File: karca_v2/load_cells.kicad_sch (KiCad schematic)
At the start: 4 parts, among them J3 Screw_Terminal_01x08, J4 Screw_Terminal_01x08, U3 MCP3208

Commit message: updated
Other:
- moved on the sheet: C6, J3, J4, U3

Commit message: Version alpha
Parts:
- added C66, C67, C68, C69: 0.1u, Capacitor_SMD:C_1206_3216Metric, symbol Device:C
- added RV1: 30k, Potentiometer_THT:Potentiometer_Bourns_3296W_Vertical, symbol Device:R_Potentiometer
- added TP6, TP7, TP8, TP9: TestPoint, TestPoint:TestPoint_Pad_D2.0mm, symbol Connector:TestPoint
- added U3: NUP4202, Package_SO:TSOP-6_1.65x3.05mm_P0.95mm, symbol Power_Protection:NUP4202
- added U4, U5: TLV9304xD, Package_SO:SO-14_3.9x8.65mm_P1.27mm, symbol Amplifier_Operational:TLV9304xD
- J4: renamed from J3; value Screw_Terminal_01x08 -> LoadCell_1_2; footprint (none) -> terminal blocks:P-2604-1108
- J5: renamed from J4; value Screw_Terminal_01x08 -> LoadCell_3_4; footprint (none) -> terminal blocks:P-2604-1108
- U2: renamed from U3; footprint (none) -> Package_SO:SOIC-16_3.9x9.9mm_P1.27mm
- renumbered C6 to C2
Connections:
- net +5V: now also C66.2, C68.2, RV1.3, U3.5, U4.4 (V+), U5.4 (V+)
- net GND: now also C66.1, C67.1, C67.2, C68.1, C69.1, C69.2, RV1.1, U3.2, U4.11 (V-), U5.11 (V-)
- net LC_Amplification/OUT: now also TP6.1, U3.6
- net LC_Amplification1/OUT: now also TP7.1, U3.4
- net LC_Amplification2/OUT: now also TP8.1, U3.1
- net LC_Amplification3/OUT: now also TP9.1, U3.3
- net DRV1_ADC: now reaches U2.5 (CH4)
- net DRV2_ADC: now reaches U2.6 (CH5)
- net DRV3_ADC: now reaches U2.7 (CH6)
- net DRV4_ADC: now reaches U2.8 (CH7)
- new net IN_AMP_VREF: RV1.2
- no-connect marks 4 -> 0
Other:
- sheet LC_Amplification ports: added INAMP_VREF; removed none
- sheet LC_Amplification1 ports: added INAMP_VREF; removed none
- sheet LC_Amplification2 ports: added INAMP_VREF; removed none
- sheet LC_Amplification3 ports: added INAMP_VREF; removed none
- moved on the sheet: C2, J4, J5, U2

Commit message: fkkkkkkkkkk
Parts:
- U3: footprint Package_SO:TSOP-6_1.65x3.05mm_P0.95mm -> Package_TO_SOT_SMD:SOT-363_SC-70-6
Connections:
- net DRV1_ADC is gone; now on net LC_Amplification/OUT: U2.5 (CH4)
- net DRV2_ADC is gone; now on net LC_Amplification1/OUT: U2.6 (CH5)
- net DRV3_ADC is gone; now on net LC_Amplification2/OUT: U2.7 (CH6)
- net DRV4_ADC is gone; now on net LC_Amplification3/OUT: U2.8 (CH7)
- net LC_Amplification/OUT: now also U3.4; no longer U2.1 (CH0), U3.6
- net LC_Amplification1/OUT: now also U3.6; no longer U2.2 (CH1), U3.4
- net LC_Amplification2/OUT: no longer U2.3 (CH2)
- net LC_Amplification3/OUT: no longer U2.4 (CH3)
- new net TC_1_ADC: U2.3 (CH2)
- new net TC_2_ADC: U2.4 (CH3)
- new net TC_3_ADC: U2.1 (CH0)
- new net TC_4_ADC: U2.2 (CH1)

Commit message: discrete traces
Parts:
- renumbered C2 to C3, C66 to C4, C68 to C5, C67 to C6, C69 to C7
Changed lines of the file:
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@@
   (symbol (lib_id "power:GND") (at 80.645 170.18 0) (unit 1)
     (in_bom yes) (on_board yes) (dnp no) (fields_autoplaced)
-    (property "Reference" "#PWR0197" (at 80.645 176.53 0)
+    (property "Reference" "#PWR028" (at 80.645 176.53 0)
       (effects (font (size 1.27 1.27)) hide)
     )
@@
       (project "karca_v2"
         (path "/29cf4797-56f2-4f57-ae95-7df639362e3c/ddbef897-b93d-4056-8606-b8e89931524a"
-          (reference "#PWR0197") (unit 1)
+          (reference "#PWR028") (unit 1)
         )
       )
@@
   (symbol (lib_id "power:GND") (at 41.275 184.15 0) (unit 1)
     (in_bom yes) (on_board yes) (dnp no) (fields_autoplaced)
-    (property "Reference" "#PWR0195" (at 41.275 190.5 0)
+    (property "Reference" "#PWR030" (at 41.275 190.5 0)
       (effects (font (size 1.27 1.27)) hide)
     )
@@
       (project "karca_v2"
         (path "/29cf4797-56f2-4f57-ae95-7df639362e3c/ddbef897-b93d-4056-8606-b8e89931524a"
-          (reference "#PWR0195") (unit 1)
+          (reference "#PWR030") (unit 1)
         )
       )
@@
   (symbol (lib_id "power:GND") (at 83.82 68.58 0) (unit 1)
     (in_bom yes) (on_board yes) (dnp no) (fields_autoplaced)
-    (property "Reference" "#PWR016" (at 83.82 74.93 0)
+    (property "Reference" "#PWR017" (at 83.82 74.93 0)
       (effects (font (size 1.27 1.27)) hide)
     )
@@
       (project "karca_v2"
         (path "/29cf4797-56f2-4f57-ae95-7df639362e3c/ddbef897-b93d-4056-8606-b8e89931524a"
-          (reference "#PWR016") (unit 1)
+          (reference "#PWR017") (unit 1)
         )
       )
@@
   (symbol (lib_id "power:+5V") (at 87.63 35.306 0) (unit 1)
     (in_bom yes) (on_board yes) (dnp no) (fields_autoplaced)
-    (property "Reference" "#PWR014" (at 87.63 39.116 0)
+    (property "Reference" "#PWR015" (at 87.63 39.116 0)
       (effects (font (size 1.27 1.27)) hide)
     )
@@
       (project "karca_v2"
         (path "/29cf4797-56f2-4f57-ae95-7df639362e3c/ddbef897-b93d-4056-8606-b8e89931524a"
-          (reference "#PWR014") (unit 1)
+          (reference "#PWR015") (unit 1)
         )
       )
@@
   (symbol (lib_id "power:+5V") (at 46.355 158.75 0) (unit 1)
     (in_bom yes) (on_board yes) (dnp no) (fields_autoplaced)
-    (property "Reference" "#PWR020" (at 46.355 162.56 0)
+    (property "Reference" "#PWR026" (at 46.355 162.56 0)
       (effects (font (size 1.27 1.27)) hide)
     )
@@
       (project "karca_v2"
         (path "/29cf4797-56f2-4f57-ae95-7df639362e3c/ddbef897-b93d-4056-8606-b8e89931524a"
-          (reference "#PWR020") (unit 1)
+          (reference "#PWR026") (unit 1)
         )
       )
@@
   (symbol (lib_id "power:+5V") (at 74.93 85.09 0) (unit 1)
     (in_bom yes) (on_board yes) (dnp no) (fields_autoplaced)
-    (property "Reference" "#PWR018" (at 74.93 88.9 0)
+    (property "Reference" "#PWR019" (at 74.93 88.9 0)
       (effects (font (size 1.27 1.27)) hide)
     )
@@
       (project "karca_v2"
         (path "/29cf4797-56f2-4f57-ae95-7df639362e3c/ddbef897-b93d-4056-8606-b8e89931524a"
-          (reference "#PWR018") (unit 1)
+          (reference "#PWR019") (unit 1)
         )
       )
@@
   (symbol (lib_id "power:GND") (at 81.28 142.24 0) (unit 1)
     (in_bom yes) (on_board yes) (dnp no) (fields_autoplaced)
-    (property "Reference" "#PWR026" (at 81.28 148.59 0)
+    (property "Reference" "#PWR025" (at 81.28 148.59 0)
       (effects (font (size 1.27 1.27)) hide)
     )
@@
       (project "karca_v2"
         (path "/29cf4797-56f2-4f57-ae95-7df639362e3c/ddbef897-b93d-4056-8606-b8e89931524a"
-          (reference "#PWR026") (unit 1)
+          (reference "#PWR025") (unit 1)
         )
       )
@@
   (symbol (lib_id "Device:C") (at 38.735 162.56 180) (unit 1)
     (in_bom yes) (on_board yes) (dnp no)
-    (property "Reference" "C66" (at 32.385 161.29 0)
+    (property "Reference" "C4" (at 32.385 161.29 0)
       (effects (font (size 1.27 1.27)) (justify right))
     )
@@
       (project "karca_v2"
         (path "/29cf4797-56f2-4f57-ae95-7df639362e3c/ddbef897-b93d-4056-8606-b8e89931524a"
-          (reference "C66") (unit 1)
+          (reference "C4") (unit 1)
         )
       )
@@
   (symbol (lib_id "Device:C") (at 245.11 66.04 90) (unit 1)
     (in_bom yes) (on_board yes) (dnp no) (fields_autoplaced)
-    (property "Reference" "C2" (at 245.11 58.42 90)
+    (property "Reference" "C3" (at 245.11 58.42 90)
       (effects (font (size 1.27 1.27)))
     )
@@
       (project "karca_v2"
         (path "/29cf4797-56f2-4f57-ae95-7df639362e3c/ddbef897-b93d-4056-8606-b8e89931524a"
-          (reference "C2") (unit 1)
+          (reference "C3") (unit 1)
         )
       )
@@
   (symbol (lib_id "power:GND") (at 80.645 186.69 0) (unit 1)
     (in_bom yes) (on_board yes) (dnp no) (fields_autoplaced)
-    (property "Reference" "#PWR0196" (at 80.645 193.04 0)
+    (property "Reference" "#PWR031" (at 80.645 193.04 0)
       (effects (font (size 1.27 1.27)) hide)
     )
@@
       (project "karca_v2"
         (path "/29cf4797-56f2-4f57-ae95-7df639362e3c/ddbef897-b93d-4056-8606-b8e89931524a"
-          (reference "#PWR0196") (unit 1)
+          (reference "#PWR031") (unit 1)
         )
       )
@@
   (symbol (lib_id "Device:C") (at 41.275 180.34 180) (unit 1)
     (in_bom yes) (on_board yes) (dnp no)
-    (property "Reference" "C67" (at 34.29 179.07 0)
+    (property "Reference" "C6" (at 34.29 179.07 0)
       (effects (font (size 1.27 1.27)) (justify right))
     )
@@
       (project "karca_v2"
         (path "/29cf4797-56f2-4f57-ae95-7df639362e3c/ddbef897-b93d-4056-8606-b8e89931524a"
-          (reference "C67") (unit 1)
+          (reference "C6") (unit 1)
         )
       )
@@
   (symbol (lib_id "power:GND") (at 252.73 68.58 0) (unit 1)
     (in_bom yes) (on_board yes) (dnp no) (fields_autoplaced)
-    (property "Reference" "#PWR017" (at 252.73 74.93 0)
+    (property "Reference" "#PWR018" (at 252.73 74.93 0)
       (effects (font (size 1.27 1.27)) hide)
     )
@@
       (project "karca_v2"
         (path "/29cf4797-56f2-4f57-ae95-7df639362e3c/ddbef897-b93d-4056-8606-b8e89931524a"
-          (reference "#PWR017") (unit 1)
+          (reference "#PWR018") (unit 1)
         )
       )
@@
   (symbol (lib_id "power:GND") (at 46.355 178.308 0) (unit 1)
     (in_bom yes) (on_board yes) (dnp no) (fields_autoplaced)
-    (property "Reference" "#PWR025" (at 46.355 184.658 0)
+    (property "Reference" "#PWR029" (at 46.355 184.658 0)
       (effects (font (size 1.27 1.27)) hide)
     )
@@
       (project "karca_v2"
         (path "/29cf4797-56f2-4f57-ae95-7df639362e3c/ddbef897-b93d-4056-8606-b8e89931524a"
-          (reference "#PWR025") (unit 1)
+          (reference "#PWR029") (unit 1)
         )
       )
@@
   (symbol (lib_id "Device:C") (at 80.645 182.88 180) (unit 1)
     (in_bom yes) (on_board yes) (dnp no)
-    (property "Reference" "C69" (at 74.295 181.61 0)
+    (property "Reference" "C7" (at 74.295 181.61 0)
       (effects (font (size 1.27 1.27)) (justify right))
     )
@@
       (project "karca_v2"
         (path "/29cf4797-56f2-4f57-ae95-7df639362e3c/ddbef897-b93d-4056-8606-b8e89931524a"
-          (reference "C69") (unit 1)
+          (reference "C7") (unit 1)
         )
       )
@@
   (symbol (lib_id "power:+5V") (at 229.87 64.77 0) (unit 1)
     (in_bom yes) (on_board yes) (dnp no) (fields_autoplaced)
-    (property "Reference" "#PWR015" (at 229.87 68.58 0)
+    (property "Reference" "#PWR016" (at 229.87 68.58 0)
       (effects (font (size 1.27 1.27)) hide)
     )
@@
       (project "karca_v2"
         (path "/29cf4797-56f2-4f57-ae95-7df639362e3c/ddbef897-b93d-4056-8606-b8e89931524a"
-          (reference "#PWR015") (unit 1)
+          (reference "#PWR016") (unit 1)
         )
       )
@@
   (symbol (lib_id "power:+5V") (at 186.69 88.9 0) (unit 1)
     (in_bom yes) (on_board yes) (dnp no) (fields_autoplaced)
-    (property "Reference" "#PWR019" (at 186.69 92.71 0)
+    (property "Reference" "#PWR020" (at 186.69 92.71 0)
       (effects (font (size 1.27 1.27)) hide)
     )
@@
       (project "karca_v2"
         (path "/29cf4797-56f2-4f57-ae95-7df639362e3c/ddbef897-b93d-4056-8606-b8e89931524a"
-          (reference "#PWR019") (unit 1)
+          (reference "#PWR020") (unit 1)
         )
       )
@@
   (symbol (lib_id "power:GND") (at 38.735 166.37 0) (unit 1)
     (in_bom yes) (on_board yes) (dnp no) (fields_autoplaced)
-    (property "Reference" "#PWR0194" (at 38.735 172.72 0)
+    (property "Reference" "#PWR027" (at 38.735 172.72 0)
       (effects (font (size 1.27 1.27)) hide)
     )
@@
       (project "karca_v2"
         (path "/29cf4797-56f2-4f57-ae95-7df639362e3c/ddbef897-b93d-4056-8606-b8e89931524a"
-          (reference "#PWR0194") (unit 1)
+          (reference "#PWR027") (unit 1)
         )
       )
@@
   (symbol (lib_id "Device:C") (at 80.645 166.37 180) (unit 1)
     (in_bom yes) (on_board yes) (dnp no)
-    (property "Reference" "C68" (at 74.295 165.1 0)
+    (property "Reference" "C5" (at 74.295 165.1 0)
       (effects (font (size 1.27 1.27)) (justify right))
     )
@@
       (project "karca_v2"
         (path "/29cf4797-56f2-4f57-ae95-7df639362e3c/ddbef897-b93d-4056-8606-b8e89931524a"
-          (reference "C68") (unit 1)
-        )
-      )
+          (reference "C5") (unit 1)
+        )
+      )

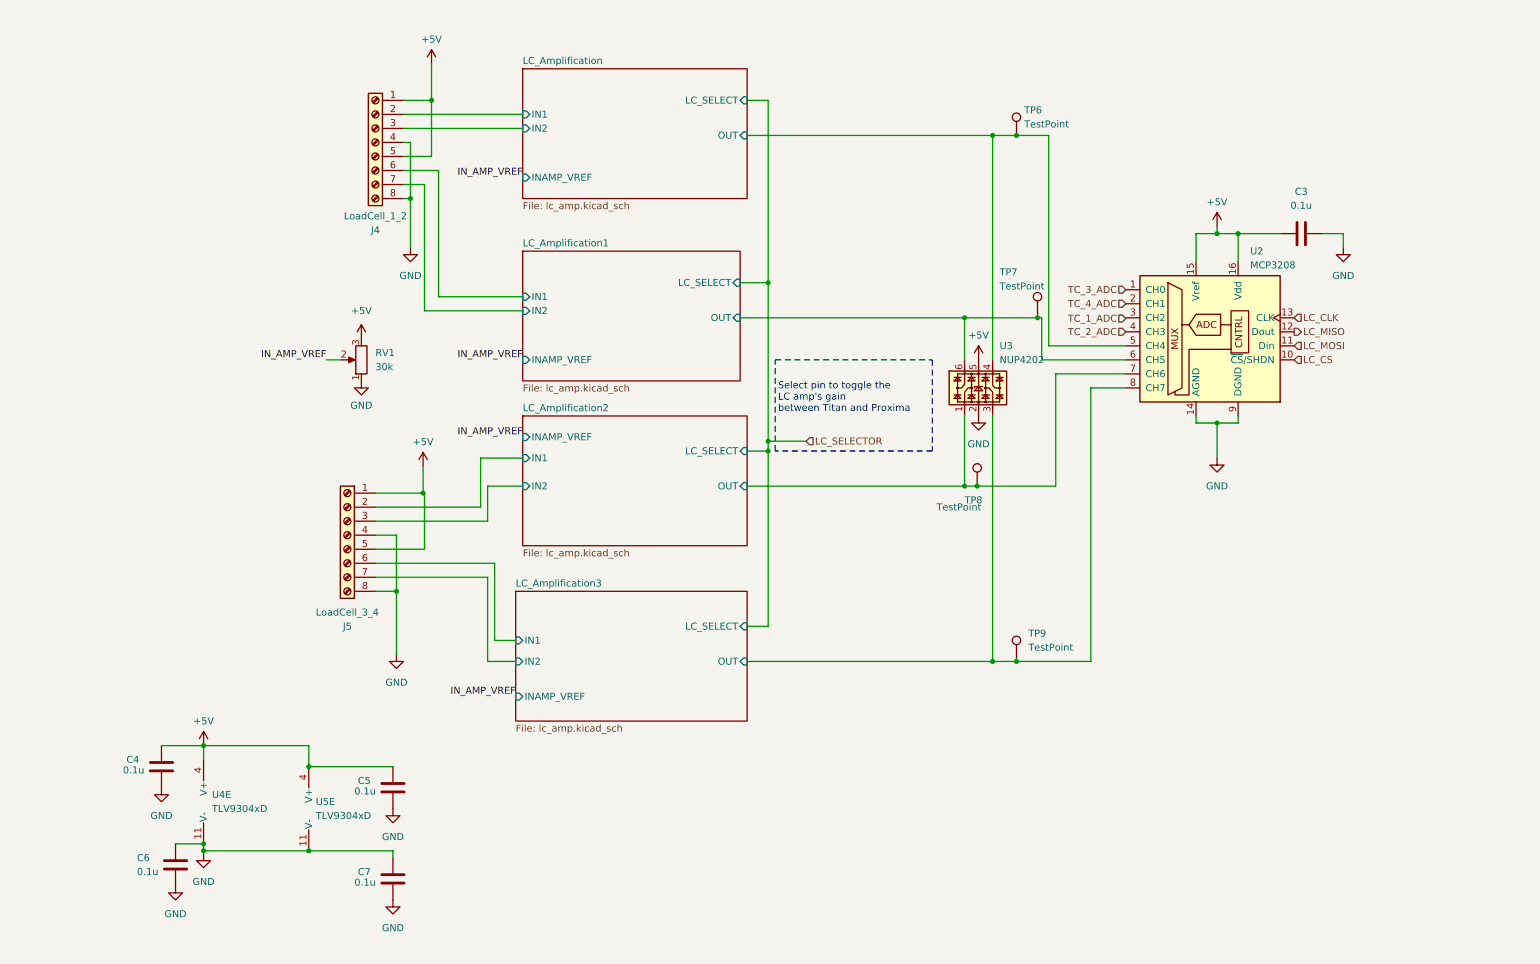
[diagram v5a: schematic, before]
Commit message: fixed TVS Diodes
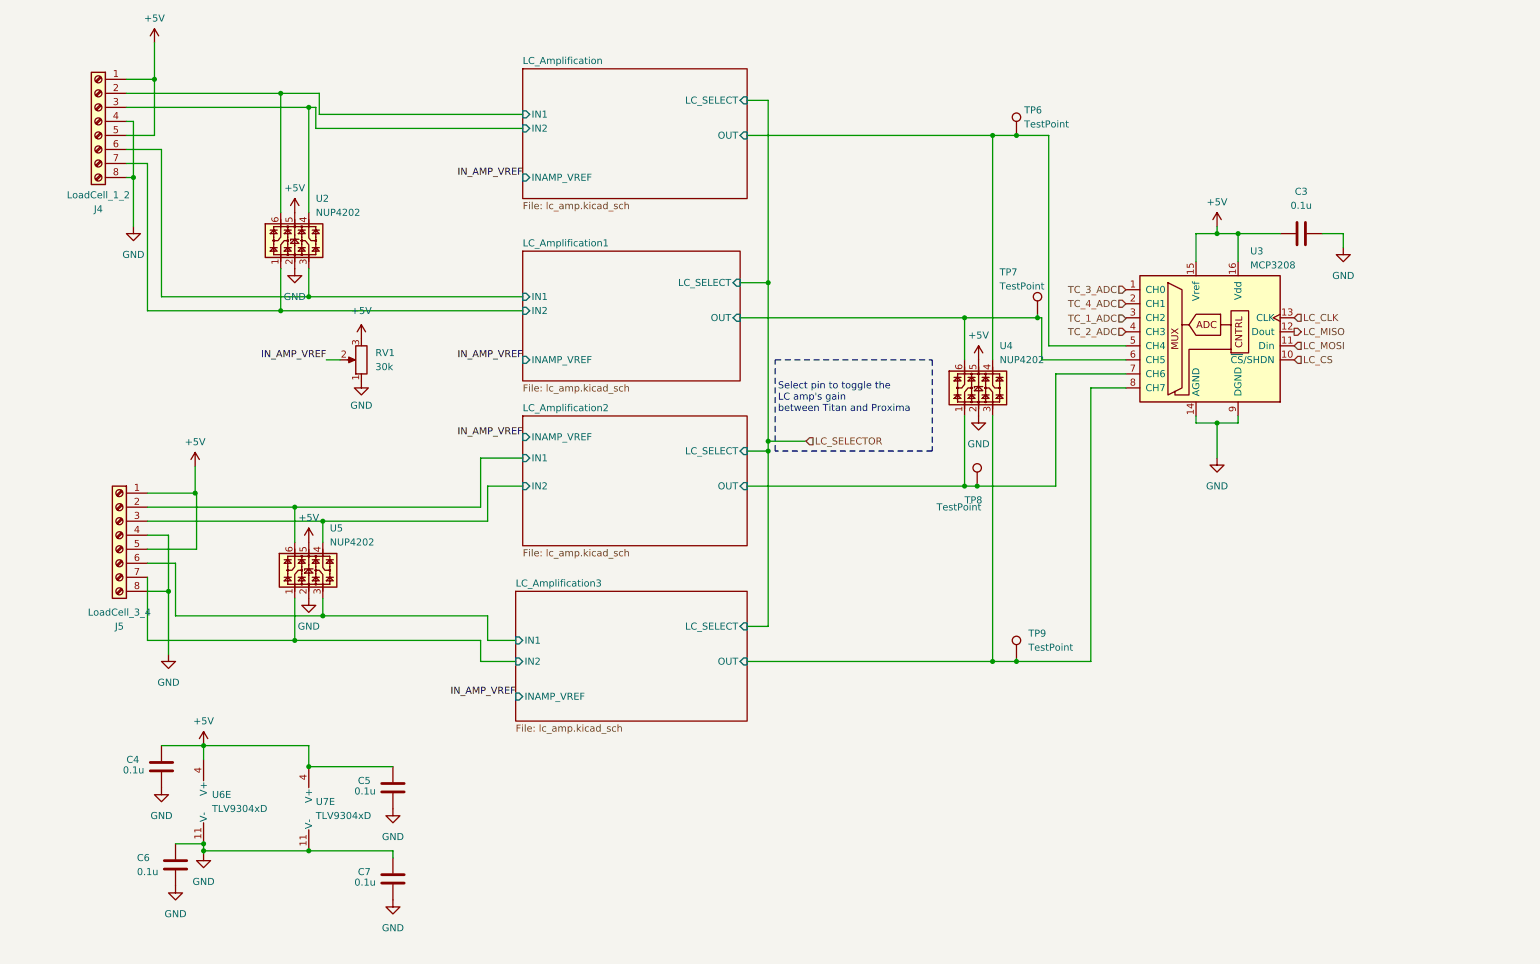
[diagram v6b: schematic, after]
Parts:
- added U2, U5: NUP4202, Package_TO_SOT_SMD:SOT-363_SC-70-6, symbol Power_Protection:NUP4202
- renumbered U2 to U3, U3 to U4, U4 to U6, U5 to U7
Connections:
- net +5V: now also U2.5, U5.5
- net GND: now also U2.2, U5.2
- net LC_Amplification/IN1: now also U2.6
- net LC_Amplification/IN2: now also U2.4
- net LC_Amplification1/IN1: now also U2.3
- net LC_Amplification1/IN2: now also U2.1
- net LC_Amplification2/IN1: now also U5.6
- net LC_Amplification2/IN2: now also U5.4
- net LC_Amplification3/IN1: now also U5.3
- net LC_Amplification3/IN2: now also U5.1
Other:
- moved on the sheet: J4, J5

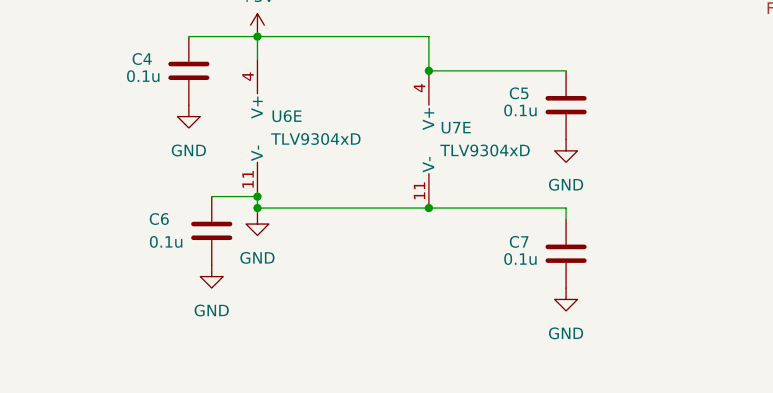
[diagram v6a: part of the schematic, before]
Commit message: Fixed ground capacitors
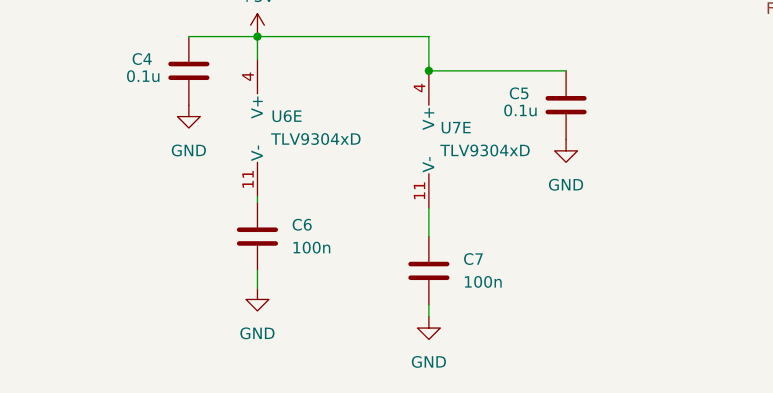
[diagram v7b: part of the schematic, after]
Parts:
- C6, C7: value 0.1u -> 100n
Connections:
- net GND: no longer C6.2, C7.2, U6.11 (V-), U7.11 (V-)
- new net: C7.2, U7.11 (V-)
- new net: C6.2, U6.11 (V-)
